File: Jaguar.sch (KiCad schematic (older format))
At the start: 27 parts, among them J2 TE-34, P1 12v-SW, P10 TPS, P11 TPS-GND, P12 O2, P13 O2-GND, P14 CRANK+, P15 CRANK-, P16 CAM+, P17 CAM-, P18 DIS-BYPASS, P19 IGN-ADVANCE, P2 12v-SW2, P20 PT3-5, P21 Inj-IN, P22 INJ-GND, P25 FUEL-, P26 Injectors, P3 GND, P31 OUT-GND, P32 OUT-12v, P4 BRV-12v, P5 GND2, P6 IAT, P7 MAT, P8 COOLANT, P9 TPS-5v

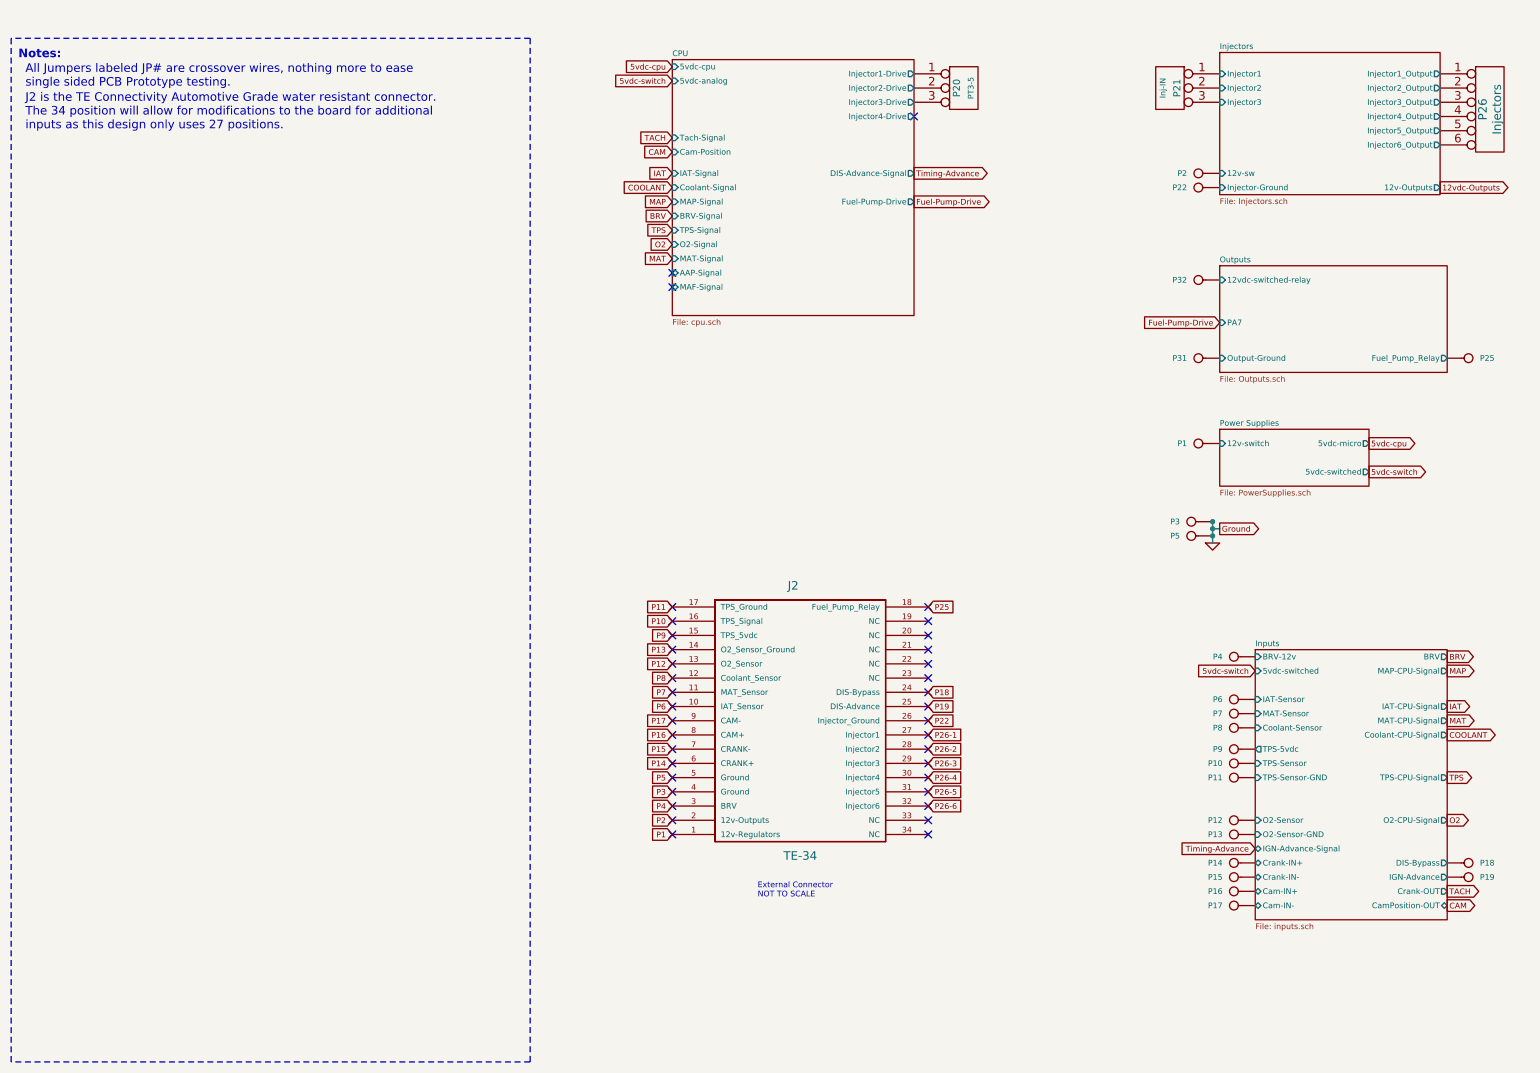
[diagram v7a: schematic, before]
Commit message: Schematics, PDF, BOM updated with latest changes
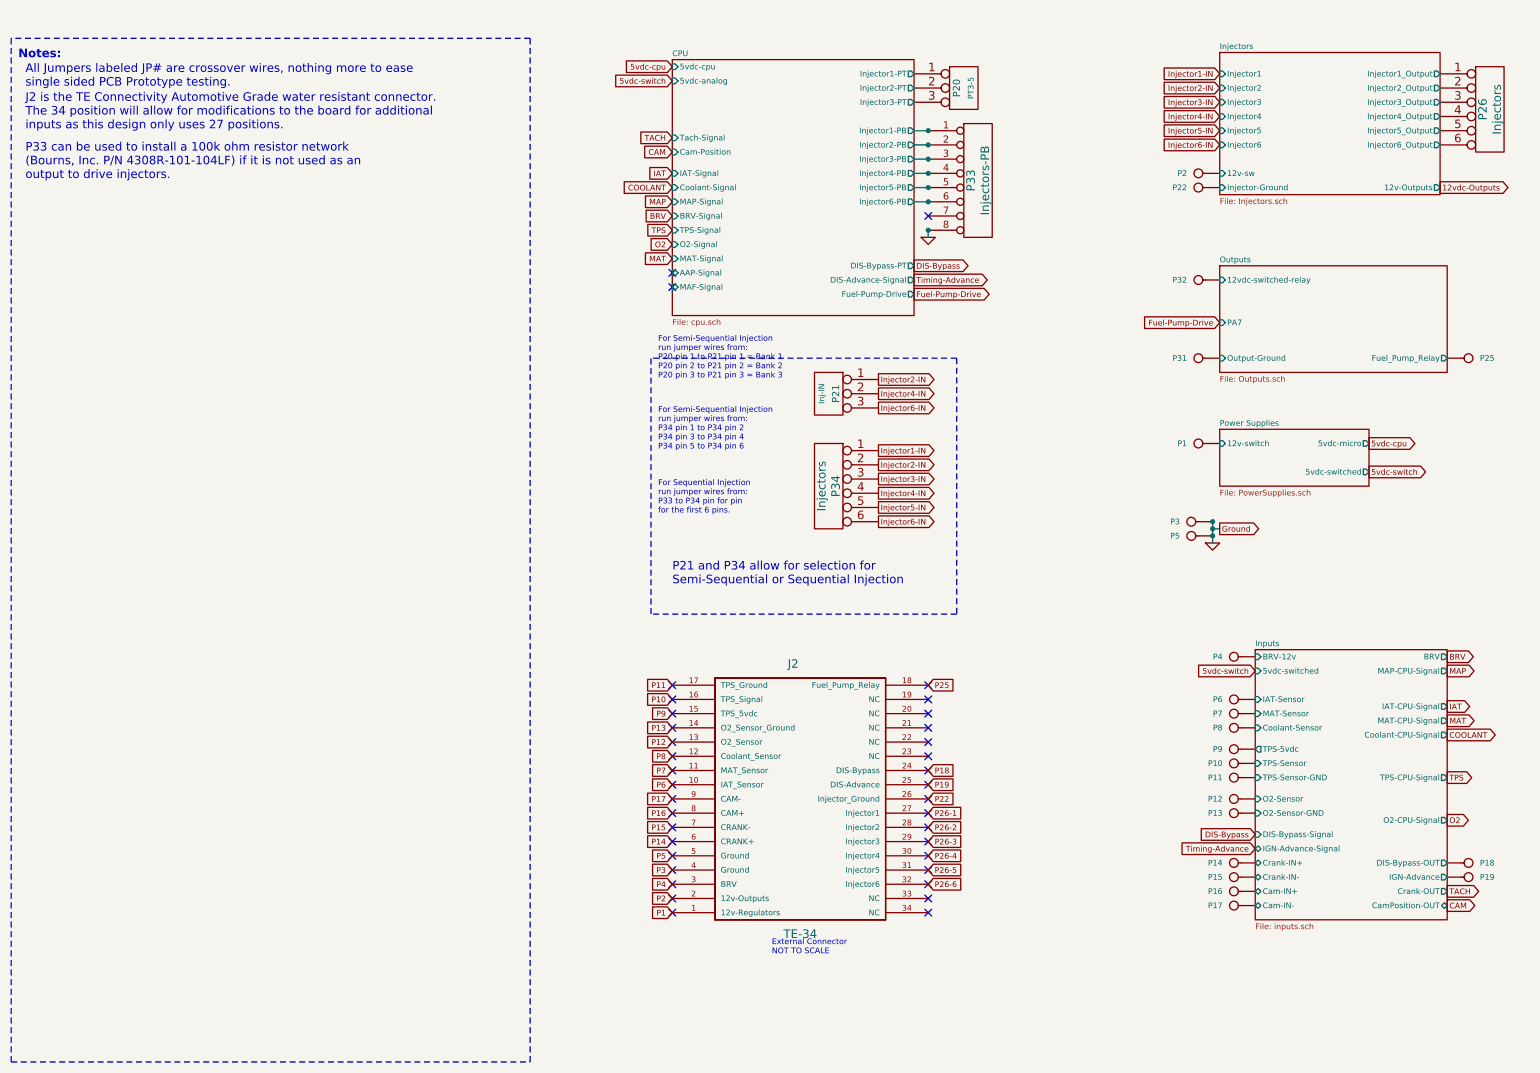
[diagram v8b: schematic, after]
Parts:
- added P33: Injectors-PB, symbol CONN_8
- added P34: Injectors, symbol CONN_6
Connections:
- net GND: now also P33.8 (P8)
- net CPU/Injector1-Drive renamed CPU/Injector1-PT
- net CPU/Injector2-Drive renamed CPU/Injector2-PT
- net CPU/Injector3-Drive renamed CPU/Injector3-PT
- net Injectors/Injector1 renamed Injector2-IN
- net Injector2-IN: now also P34.2
- net Injectors/Injector2 renamed Injector4-IN
- net Injector4-IN: now also P34.4
- net Injectors/Injector3 renamed Injector6-IN
- net Injector6-IN: now also P34.6
- net Inputs/DIS-Bypass renamed Inputs/DIS-Bypass-OUT
- new net CPU/Injector1-PB: P33.1 (P1)
- new net CPU/Injector2-PB: P33.2 (P2)
- new net CPU/Injector3-PB: P33.3 (P3)
- new net CPU/Injector4-PB: P33.4 (P4)
- new net CPU/Injector5-PB: P33.5 (P5)
- new net CPU/Injector6-PB: P33.6 (P6)
- new net Injector1-IN: P34.1
- new net Injector3-IN: P34.3
- new net Injector5-IN: P34.5
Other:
- note added: "For Semi-Sequential Injection \nrun jumper wires from: \nP20 pin 1 to P21 pin 1 = Bank 1\nP20 pin 2 to P21 pin 2 = Bank 2\nP20 pin 3 to P21 pin 3 = Bank 3"
- note added: "For Semi-Sequential Injection\nrun jumper wires from:\nP34 pin 1 to P34 pin 2\nP34 pin 3 to P34 pin 4\nP34 pin 5 to P34 pin 6"
- note added: "For Sequential Injection\nrun jumper wires from:\nP33 to P34 pin for pin\nfor the first 6 pins.\n"
- note added: "P21 and P34 allow for selection for\nSemi-Sequential or Sequential Injection"
- note added: "P33 can be used to install a 100k ohm resistor network \n(Bourns, Inc. P/N 4308R-101-104LF) if it is not used as an\noutput to drive injectors."
- moved on the sheet: J2, P12, P13, P21
